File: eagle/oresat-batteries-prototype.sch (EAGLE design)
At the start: 81 parts, among them Q10 BSS84, Q11 BSS84, Q12 Si7625DN, Q13 Si7625DN, Q14 Si7625DN, Q15 Si7625DN, Q16 Si7625DN, Q2 Si7625DN, Q9 Si7625DN, U10 LTC4412, U11 S-8209AAA-T8T1U, U12 S-8209AAA-T8T1U, U2 MAX17205G, U9 LTC4412

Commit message: v1.0 of the battery pack prototype board
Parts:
- removed T1, T2, T3, T4, T5, T6: (no value), zetex:NMOSSOT23
- added Q1, Q3, Q4, Q5, Q6, Q7: PMV45EN, Tova:PMV45EN
- added TP1, TP3, TP4, TP5: TEST-POINT, Tova:TEST-POINT
- Q10, Q11: value BSS84 -> NTR4101P; device Transistor:BSS84 -> Tova:NTR4101P
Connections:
- net !FAST-CHARGE-PK1: now also Q1.D; no longer T2.D
- net CHARGE-DISABLE: now also Q6.G; no longer T6.G
- net CSP-PK1: now also Q3.S, Q4.S, Q5.S, Q6.S, Q7.S, TP3.1; no longer T1.S, T3.S, T4.S, T5.S, T6.S
- net DISCHARGE-DISABLE: now also Q7.G; no longer T5.G
- net FAST-CHARGE-PK1: now also Q1.G; no longer T2.G
- net GND: now also Q1.S; no longer T2.S
- net N$1: now also Q5.D; no longer T4.D
- net N$10: now also Q3.D; no longer T3.D
- net N$11: now also Q4.G, Q7.D; no longer T1.G, T5.D
- net N$42: now also TP4.1
- net N$5: now also Q4.D; no longer T1.D
- net N$51: now also Q3.G, Q6.D; no longer T3.G, T6.D
- net N$53: now also TP1.1
- net N$54: now also TP5.1
- net OPD-PK1-DISABLE: now also Q5.G; no longer T4.G
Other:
- note added: "OreSat Prototype Battery Pack"
- note removed: "OreSat battery Card - Battery Pack 1"

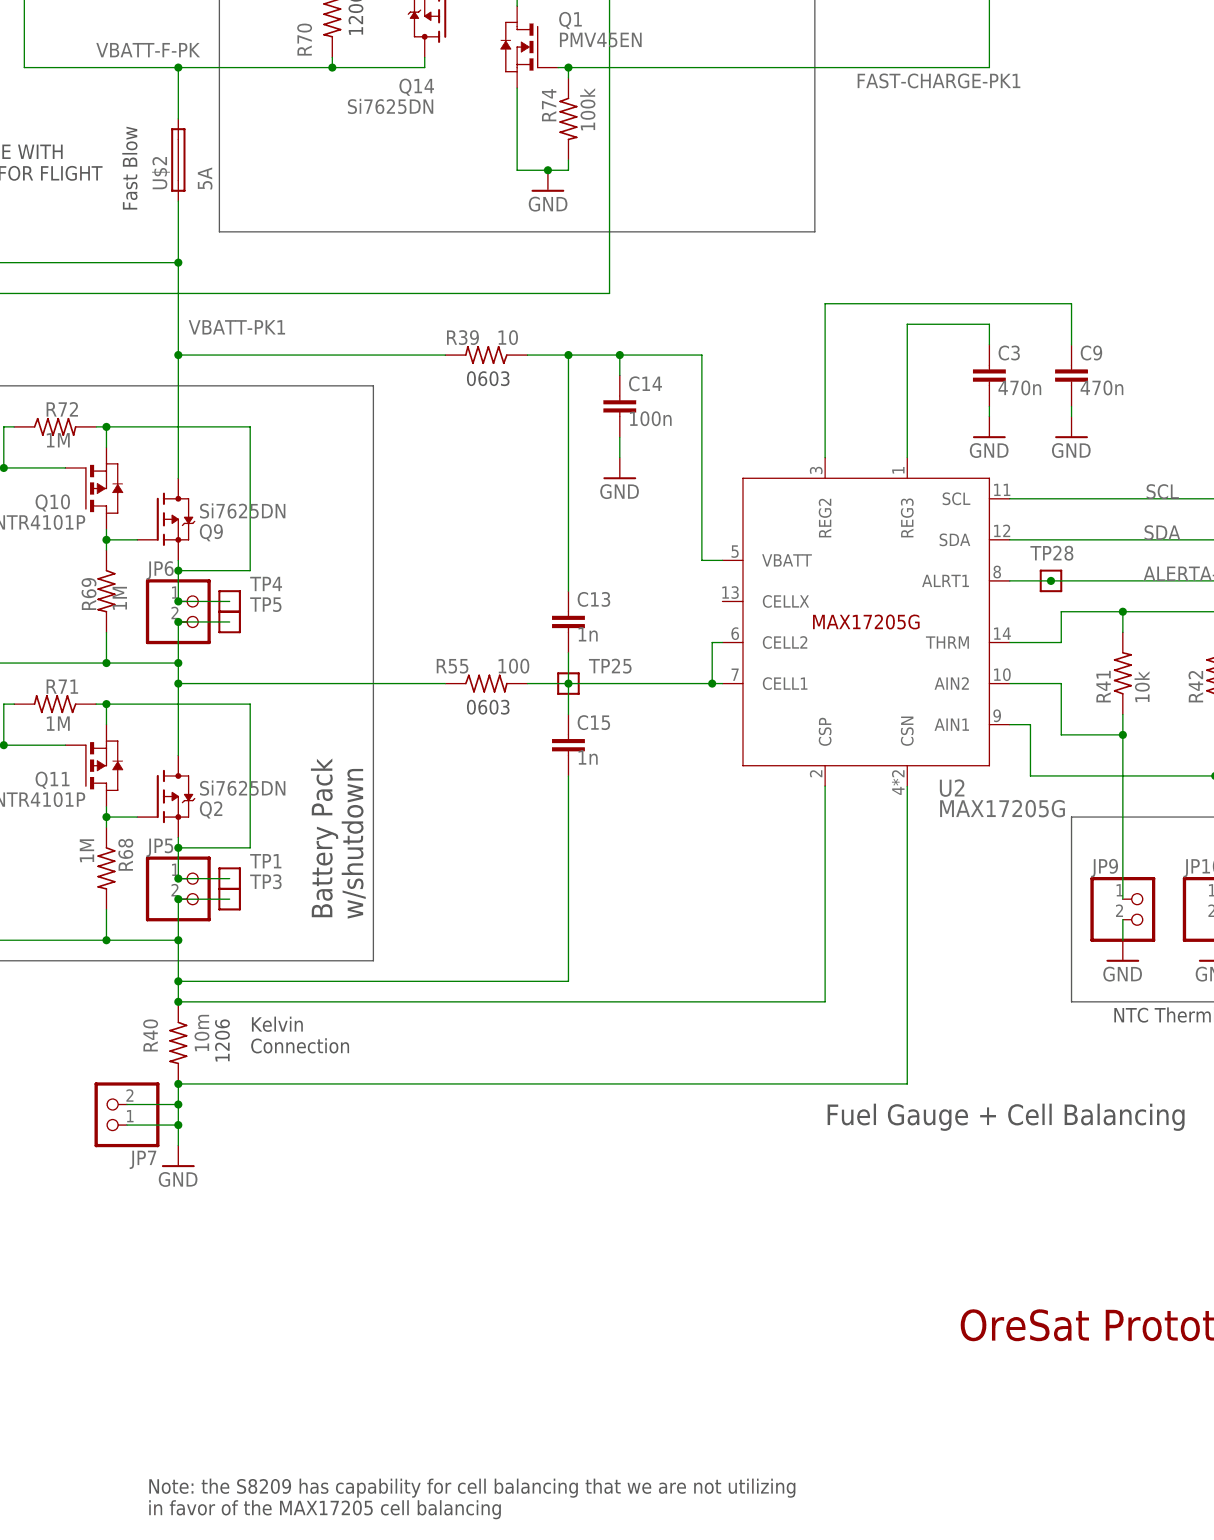
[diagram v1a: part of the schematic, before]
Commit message: Finalized battery prototype, choose parts, made BOM, ordered!
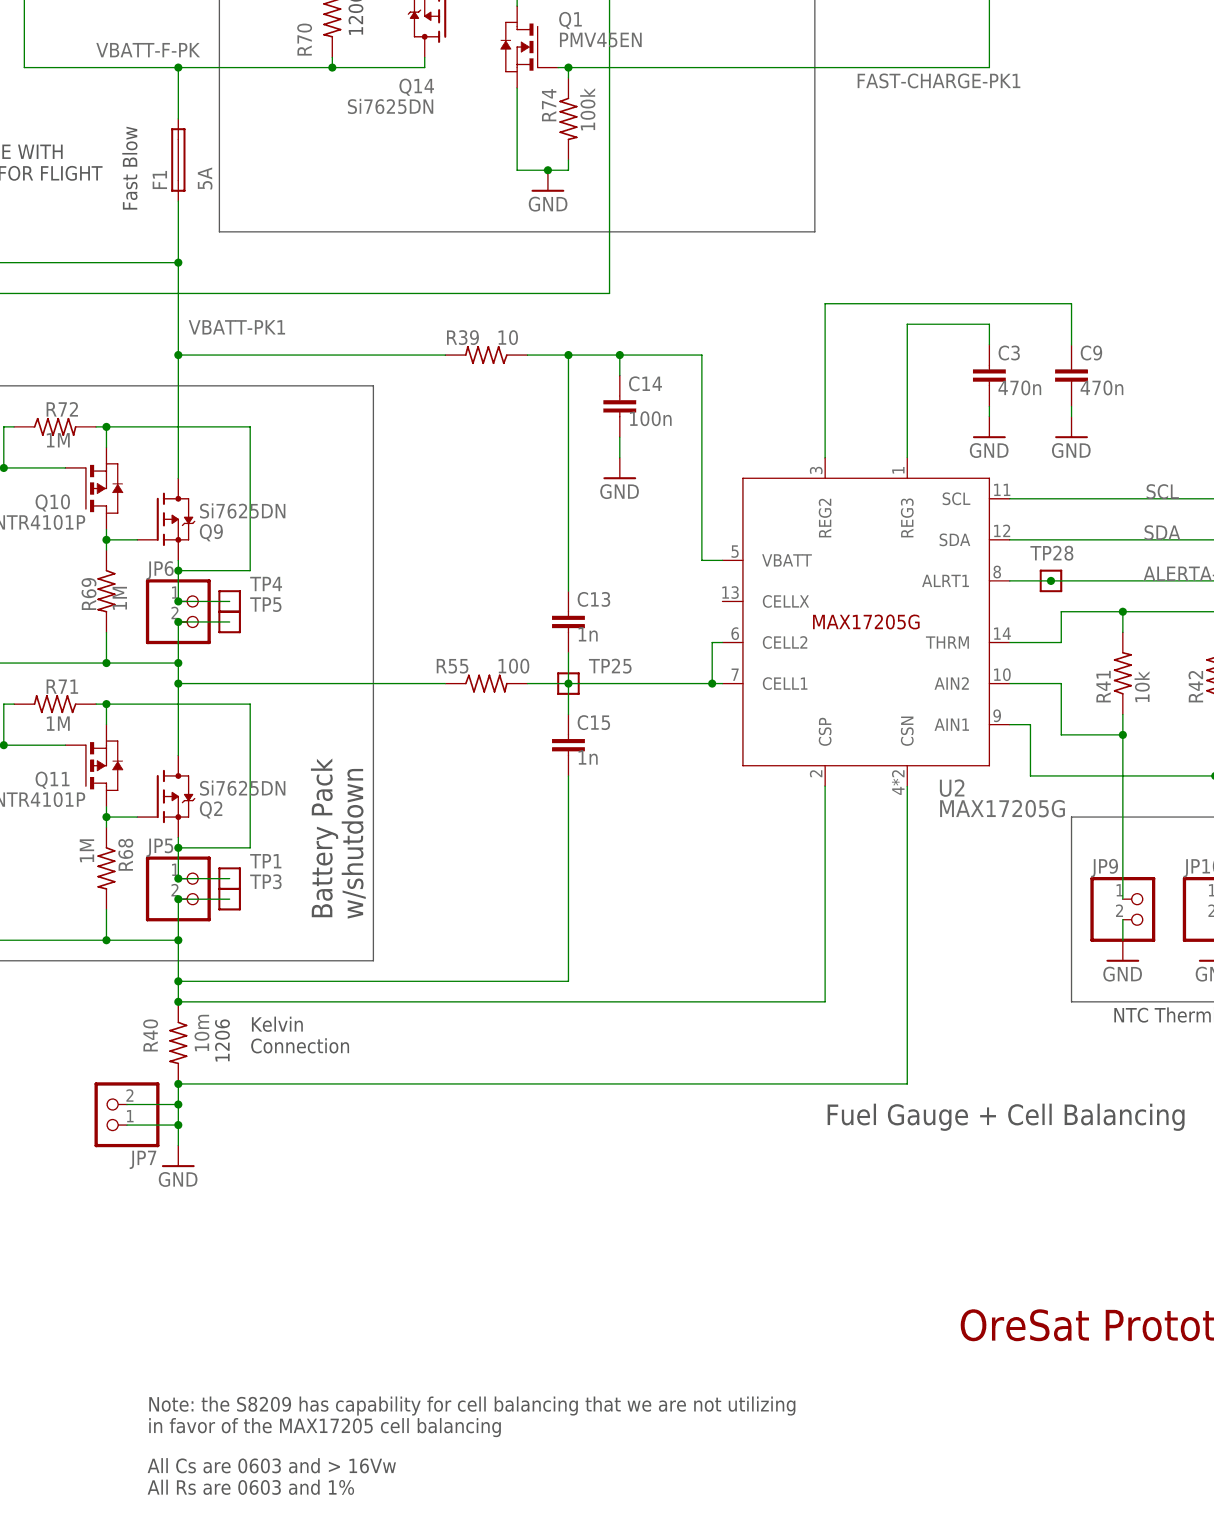
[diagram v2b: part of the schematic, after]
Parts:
- D1, D10, D11, D4: MFR (none) -> Micro Commercial Co; MPN (none) -> 1N4148WL2-TP
- F1: DPN P15125CT-ND -> (none); MFR (none) -> Panasonic; VENDOR Digi-Key -> (none)
- Q1, Q3, Q4, Q5, Q6, Q7: MFR (none) -> Diodes Inc; MPN (none) -> DMG2302UK-7
- Q10, Q11: MFR (none) -> Diodes Inc; MPN (none) -> DMG3401LSN-7
- Q12, Q13, Q14, Q15, Q16, Q2, Q9: MFR (none) -> Vishay Siliconix; MPN (none) -> SI7625DN-T1-GE3
- R41: DISTRIBUTOR Digi-key -> (none); DPN RNCP0603FTD10K0CT-ND -> (none); MPN RNCP0603FTD10K0 -> (none)
- U10, U9: MFR (none) -> Linear Technology; MPN (none) -> LTC4412HS6#TRMPBF
- U2: MFR (none) -> Maxim Integrated; MPN (none) -> MAX17205G+T
- renumbered U$2 to F1
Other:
- note added: "All Cs are 0603 and > 16Vw All Rs are 0603 and 1%"
- note removed: "0603"
